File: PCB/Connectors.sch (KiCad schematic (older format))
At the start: 2 parts, among them P3 CONTROL, P4 MAIN_CONN

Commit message: Libraries and footprints adjustments. New connectors (4 pins main, 2 pins debug and 6 pins isp). New source input cap.
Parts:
- added P?: DEBUG TX/RX, symbol CONN_01X02
- added P?: ISP, symbol CONN_02X03
- P4: footprint Connectors_Molex:Molex_MiniFit-JR-5569-08A1_2x04x4.20mm_Angled -> Connectors_Molex:Molex_MiniFit-JR-5556-06A_2x03x4.20mm_Straight; symbol CONN_01X08 -> CONN_01X06
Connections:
- net +5V: now also P4.6 (P6), P?.2 (P2); no longer P4.1 (P1), P4.8 (P8)
- net CH0_OUT: now also P4.1 (P1); no longer P4.2 (P2)
- net CH0_PEDAL_SIG: now also P4.4 (P4); no longer P4.6 (P6)
- net CH1_OUT: now also P4.2 (P2); no longer P4.3 (P3)
- net CH1_PEDAL_SIG: now also P4.5 (P5); no longer P4.7 (P7)
- net GNDREF: now also P4.3 (P3), P?.6 (P6); no longer P4.4 (P4), P4.5 (P5)
- new net MISO: P?.1 (P1)
- new net MOSI: P?.4 (P4)
- new net RESET: P?.5 (P5)
- new net RX: P?.2 (P2)
- new net SCK: P?.3 (P3)
- new net TX: P?.1 (P1)
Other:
- moved on the sheet: P3
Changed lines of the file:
@@
 EESchema Schematic File Version 2
-LIBS:ArduBooster-rescue
 LIBS:power
 LIBS:device
@@
 Rev "1.0"
 Comp ""
-Comment1 ""
+Comment1 "Board connectors"
 Comment2 ""
 Comment3 ""
@@
 L CONN_01X05 P3
 U 1 1 54D7F0D9
-P 8200 3550
-F 0 "P3" H 8200 3850 50  0000 C CNN
-F 1 "CONTROL" V 8300 3550 50  0000 C CNN
-F 2 "Connect:Wafer_Horizontal15x5.8x7RM2.5-5" H 8200 3550 60  0001 C CNN
-F 3 "" H 8200 3550 60  0000 C CNN
-	1    8200 3550
+P 8200 4400
+F 0 "P3" H 8200 4700 50  0000 C CNN
+F 1 "CONTROL" V 8300 4400 50  0000 C CNN
+F 2 "Connect:Wafer_Horizontal15x5.8x7RM2.5-5" H 8200 4400 60  0001 C CNN
+F 3 "" H 8200 4400 60  0000 C CNN
+	1    8200 4400
 	1    0    0    1
 $EndComp
@@
 L GNDREF #PWR01
 U 1 1 54D7F247
-P 7850 3900
-F 0 "#PWR01" H 7850 3650 60  0001 C CNN
-F 1 "GNDREF" H 7850 3750 60  0000 C CNN
-F 2 "" H 7850 3900 60  0000 C CNN
-F 3 "" H 7850 3900 60  0000 C CNN
-	1    7850 3900
-	1    0    0    -1
-$EndComp
-Wire Wire Line
-	7850 3900 7850 3750
-Wire Wire Line
-	7850 3750 8000 3750
+P 7850 4750
+F 0 "#PWR01" H 7850 4500 60  0001 C CNN
+F 1 "GNDREF" H 7850 4600 60  0000 C CNN
+F 2 "" H 7850 4750 60  0000 C CNN
+F 3 "" H 7850 4750 60  0000 C CNN
+	1    7850 4750
+	1    0    0    -1
+$EndComp
+Wire Wire Line
+	7850 4750 7850 4600
+Wire Wire Line
+	7850 4600 8000 4600
 $Comp
 L +5V #PWR02
 U 1 1 54D7F26C
-P 7850 3200
-F 0 "#PWR02" H 7850 3050 60  0001 C CNN
-F 1 "+5V" H 7850 3340 60  0000 C CNN
-F 2 "" H 7850 3200 60  0000 C CNN
-F 3 "" H 7850 3200 60  0000 C CNN
-	1    7850 3200
-	1    0    0    -1
-$EndComp
-Wire Wire Line
-	8000 3350 7850 3350
-Wire Wire Line
-	7850 3350 7850 3200
-Wire Wire Line
-	7700 3650 8000 3650
-Wire Wire Line
-	7700 3550 8000 3550
-Text HLabel 7700 3450 0    60   Input ~ 0
+P 7850 4050
+F 0 "#PWR02" H 7850 3900 60  0001 C CNN
+F 1 "+5V" H 7850 4190 60  0000 C CNN
+F 2 "" H 7850 4050 60  0000 C CNN
+F 3 "" H 7850 4050 60  0000 C CNN
+	1    7850 4050
+	1    0    0    -1
+$EndComp
+Wire Wire Line
+	8000 4200 7850 4200
+Wire Wire Line
+	7850 4200 7850 4050
+Wire Wire Line
+	7700 4500 8000 4500
+Wire Wire Line
+	7700 4400 8000 4400
+Text HLabel 7700 4300 0    60   Input ~ 0
 SWITCH
 Wire Wire Line
-	7700 3450 8000 3450
-Text HLabel 7700 3650 0    60   Output ~ 0
+	7700 4300 8000 4300
+Text HLabel 7700 4500 0    60   Output ~ 0
 LED1
-Text HLabel 7700 3550 0    60   Output ~ 0
+Text HLabel 7700 4400 0    60   Output ~ 0
 LED2
-Text HLabel 4150 3650 2    60   Output ~ 0
+Text HLabel 4150 4500 2    60   Output ~ 0
 CH1_OUT
-Text HLabel 4150 3750 2    60   Output ~ 0
+Text HLabel 4150 4600 2    60   Output ~ 0
 CH0_OUT
-Text HLabel 4150 3250 2    60   Input ~ 0
+Text HLabel 4150 4200 2    60   Input ~ 0
 CH1_PEDAL_SIG
-Text HLabel 4150 3350 2    60   Input ~ 0
+Text HLabel 4150 4300 2    60   Input ~ 0
 CH0_PEDAL_SIG
 $Comp
-L CONN_01X08 P4
+L CONN_01X06 P4
 U 1 1 54E8D924
-P 3450 3500
-F 0 "P4" H 3450 3950 50  0000 C CNN
-F 1 "MAIN_CONN" V 3550 3500 50  0000 C CNN
-F 2 "Connectors_Molex:Molex_MiniFit-JR-5569-08A1_2x04x4.20mm_Angled" H 3450 3500 60  0001 C CNN
-F 3 "" H 3450 3500 60  0000 C CNN
-	1    3450 3500
+P 3450 4350
+F 0 "P4" H 3450 4800 50  0000 C CNN
+F 1 "MAIN_CONN" V 3550 4350 50  0000 C CNN
+F 2 "Connectors_Molex:Molex_MiniFit-JR-5556-06A_2x03x4.20mm_Straight" H 3450 4350 60  0001 C CNN
+F 3 "" H 3450 4350 60  0000 C CNN
+	1    3450 4350
 	-1   0    0    1
 $EndComp
@@
 L +5V #PWR03
 U 1 1 54E8E644
-P 3850 3000
-F 0 "#PWR03" H 3850 2850 60  0001 C CNN
-F 1 "+5V" H 3850 3140 60  0000 C CNN
-F 2 "" H 3850 3000 60  0000 C CNN
-F 3 "" H 3850 3000 60  0000 C CNN
-	1    3850 3000
+P 3850 3850
+F 0 "#PWR03" H 3850 3700 60  0001 C CNN
+F 1 "+5V" H 3850 3990 60  0000 C CNN
+F 2 "" H 3850 3850 60  0000 C CNN
+F 3 "" H 3850 3850 60  0000 C CNN
+	1    3850 3850
 	1    0    0    -1
 $EndComp
@@
 L PWR_FLAG #FLG04
 U 1 1 54E8E658
-P 4100 3000
-F 0 "#FLG04" H 4100 3095 30  0001 C CNN
-F 1 "PWR_FLAG" H 4100 3180 30  0000 C CNN
-F 2 "" H 4100 3000 60  0000 C CNN
-F 3 "" H 4100 3000 60  0000 C CNN
-	1    4100 3000
-	1    0    0    -1
-$EndComp
-Wire Wire Line
-	3650 3150 4100 3150
-Wire Wire Line
-	3850 3000 3850 3850
-Wire Wire Line
-	4100 3150 4100 3000
-Connection ~ 3850 3150
-Wire Wire Line
-	3850 3850 3650 3850
+P 4100 3850
+F 0 "#FLG04" H 4100 3945 30  0001 C CNN
+F 1 "PWR_FLAG" H 4100 4030 30  0000 C CNN
+F 2 "" H 4100 3850 60  0000 C CNN
+F 3 "" H 4100 3850 60  0000 C CNN
+	1    4100 3850
+	1    0    0    -1
+$EndComp
 $Comp
 L GNDREF #PWR05
 U 1 1 54E8E6DA
-P 3800 4050
-F 0 "#PWR05" H 3800 3800 60  0001 C CNN
-F 1 "GNDREF" H 3800 3900 60  0000 C CNN
-F 2 "" H 3800 4050 60  0000 C CNN
-F 3 "" H 3800 4050 60  0000 C CNN
-	1    3800 4050
+P 3800 4900
+F 0 "#PWR05" H 3800 4650 60  0001 C CNN
+F 1 "GNDREF" H 3800 4750 60  0000 C CNN
+F 2 "" H 3800 4900 60  0000 C CNN
+F 3 "" H 3800 4900 60  0000 C CNN
+	1    3800 4900
 	1    0    0    -1
 $EndComp
@@
 L PWR_FLAG #FLG06
 U 1 1 54E8E6F6
-P 4100 4050
-F 0 "#FLG06" H 4100 4145 30  0001 C CNN
-F 1 "PWR_FLAG" H 4100 4230 30  0000 C CNN
-F 2 "" H 4100 4050 60  0000 C CNN
-F 3 "" H 4100 4050 60  0000 C CNN
-	1    4100 4050
+P 4100 4900
+F 0 "#FLG06" H 4100 4995 30  0001 C CNN
+F 1 "PWR_FLAG" H 4100 5080 30  0000 C CNN
+F 2 "" H 4100 4900 60  0000 C CNN
+F 3 "" H 4100 4900 60  0000 C CNN
+	1    4100 4900
 	-1   0    0    1
 $EndComp
 Wire Wire Line
-	4100 4050 4100 4000
-Wire Wire Line
-	4100 4000 3800 4000
-Wire Wire Line
-	3800 3450 3800 4050
-Wire Wire Line
-	3650 3450 3800 3450
-Connection ~ 3800 4000
-Wire Wire Line
-	3650 3550 3800 3550
-Connection ~ 3800 3550
-Wire Wire Line
-	4150 3250 3650 3250
-Wire Wire Line
-	3650 3350 4150 3350
-Wire Wire Line
-	4150 3650 3650 3650
-Wire Wire Line
-	4150 3750 3650 3750
+	3650 4200 4150 4200
+Wire Wire Line
+	4150 4500 3650 4500
+Wire Wire Line
+	4150 4600 3650 4600
+Wire Wire Line
+	3650 4400 3800 4400
+Wire Wire Line
+	3800 4400 3800 4900
+Wire Wire Line
+	4100 4900 4100 4850
+Wire Wire Line
+	4100 4850 3800 4850
+Connection ~ 3800 4850
+Wire Wire Line
+	3650 4300 4150 4300
+Wire Wire Line
+	3850 3850 3850 4100
+Wire Wire Line
+	3850 4100 3650 4100
+Wire Wire Line
+	4100 3850 4100 3950
+Wire Wire Line
+	4100 3950 3850 3950
+Connection ~ 3850 3950
+$Comp
+L CONN_01X02 P?
+U 1 1 57BCD0AF
+P 8050 2650
+F 0 "P?" H 8050 2800 50  0000 C CNN
+F 1 "DEBUG TX/RX" V 8150 2650 50  0000 C CNN
+F 2 "" H 8050 2650 50  0000 C CNN
+F 3 "" H 8050 2650 50  0000 C CNN
+	1    8050 2650
+	1    0    0    -1
+$EndComp
+$Comp
+L CONN_02X03 P?
+U 1 1 57BCD0E6
+P 3850 2700
+F 0 "P?" H 3850 2900 50  0000 C CNN
+F 1 "ISP" H 3850 2500 50  0000 C CNN
+F 2 "" H 3850 1500 50  0000 C CNN
+F 3 "" H 3850 1500 50  0000 C CNN
+	1    3850 2700
+	1    0    0    -1
+$EndComp
+$Comp
+L +5V #PWR?
+U 1 1 57BCD18D
+P 4200 2500
+F 0 "#PWR?" H 4200 2350 60  0001 C CNN
+F 1 "+5V" H 4200 2640 60  0000 C CNN
+F 2 "" H 4200 2500 60  0000 C CNN
+F 3 "" H 4200 2500 60  0000 C CNN
+	1    4200 2500
+	1    0    0    -1
+$EndComp
+$Comp
+L GNDREF #PWR?
+U 1 1 57BCD1A8
+P 4200 2900
+F 0 "#PWR?" H 4200 2650 60  0001 C CNN
+F 1 "GNDREF" H 4200 2750 60  0000 C CNN
+F 2 "" H 4200 2900 60  0000 C CNN
+F 3 "" H 4200 2900 60  0000 C CNN
+	1    4200 2900
+	1    0    0    -1
+$EndComp
+Wire Wire Line
+	4100 2800 4200 2800
+Wire Wire Line
+	4200 2800 4200 2900
+Wire Wire Line
+	4200 2500 4200 2600
+Wire Wire Line
+	4200 2600 4100 2600
+Text HLabel 3200 2800 0    60   Output ~ 0
+RESET
+Wire Wire Line
+	3600 2800 3200 2800
+Text HLabel 3200 2700 0    60   Output ~ 0
+SCK
+Text HLabel 3200 2600 0    60   Input ~ 0
+MISO
+Wire Wire Line
+	3200 2600 3600 2600
+Wire Wire Line
+	3200 2700 3600 2700
+Text HLabel 4500 2700 2    60   Output ~ 0
+MOSI
+Wire Wire Line
+	4500 2700 4100 2700
+Text HLabel 7600 2600 0    60   Input ~ 0
+TX
+Wire Wire Line
+	7600 2600 7850 2600
+Text HLabel 7600 2700 0    60   Output ~ 0
+RX
+Wire Wire Line
+	7600 2700 7850 2700
 $EndSCHEMATC

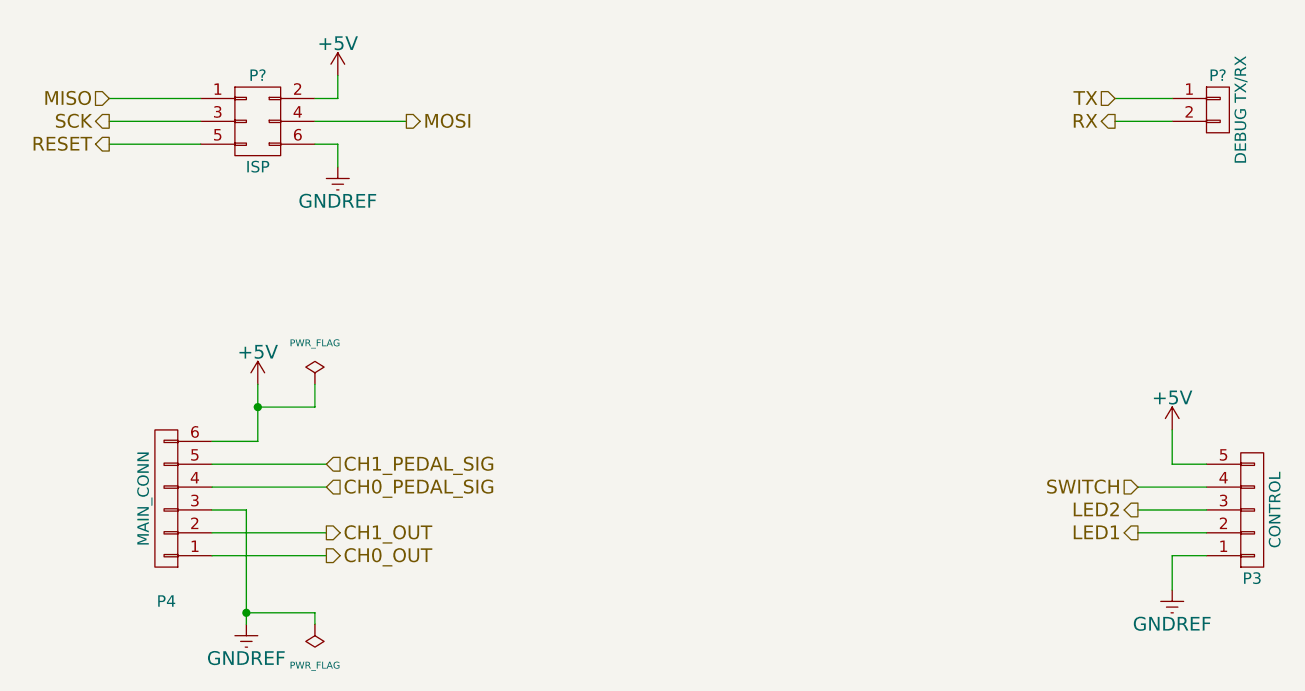
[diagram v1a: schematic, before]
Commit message: New connectors connection. Labels corrections (direction).
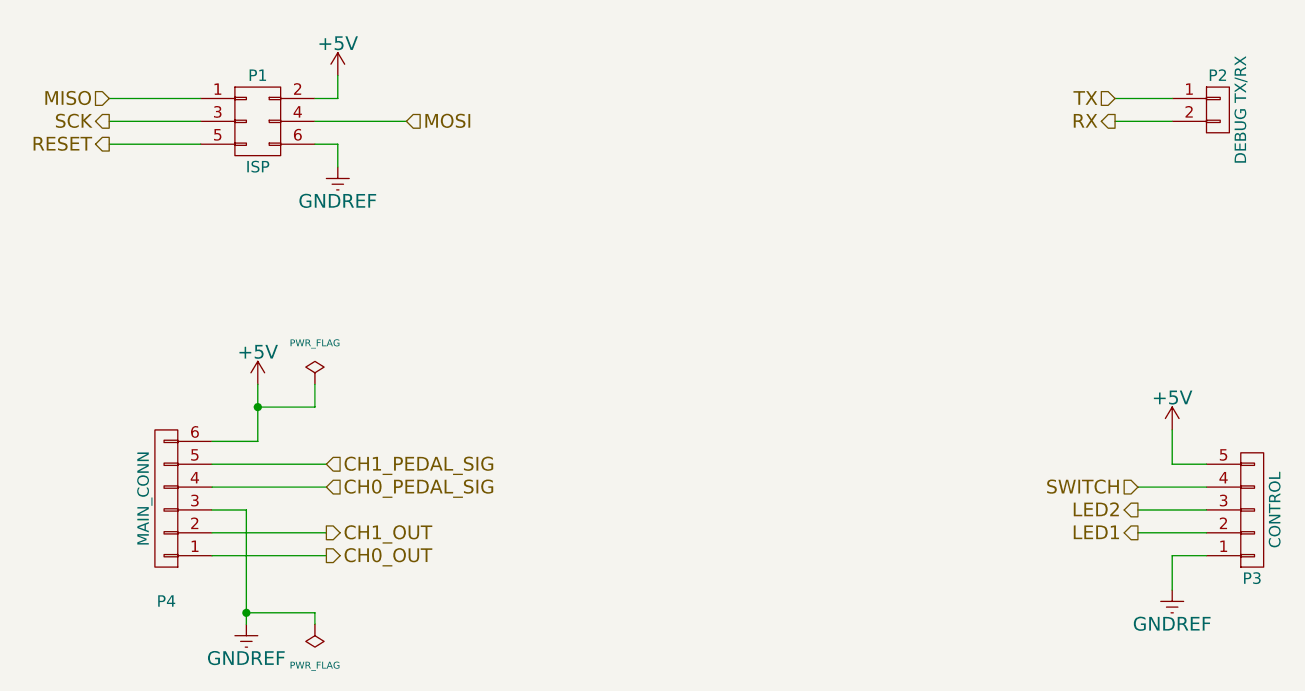
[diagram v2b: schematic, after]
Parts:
- gave numbers to parts that had none: 2
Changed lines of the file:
@@
 Connection ~ 3850 3950
 $Comp
-L CONN_01X02 P?
+L CONN_01X02 P2
 U 1 1 57BCD0AF
 P 8050 2650
-F 0 "P?" H 8050 2800 50  0000 C CNN
+F 0 "P2" H 8050 2800 50  0000 C CNN
 F 1 "DEBUG TX/RX" V 8150 2650 50  0000 C CNN
 F 2 "" H 8050 2650 50  0000 C CNN
@@
 $EndComp
 $Comp
-L CONN_02X03 P?
+L CONN_02X03 P1
 U 1 1 57BCD0E6
 P 3850 2700
-F 0 "P?" H 3850 2900 50  0000 C CNN
+F 0 "P1" H 3850 2900 50  0000 C CNN
 F 1 "ISP" H 3850 2500 50  0000 C CNN
 F 2 "" H 3850 1500 50  0000 C CNN
@@
 $EndComp
 $Comp
-L +5V #PWR?
+L +5V #PWR07
 U 1 1 57BCD18D
 P 4200 2500
-F 0 "#PWR?" H 4200 2350 60  0001 C CNN
+F 0 "#PWR07" H 4200 2350 60  0001 C CNN
 F 1 "+5V" H 4200 2640 60  0000 C CNN
 F 2 "" H 4200 2500 60  0000 C CNN
@@
 $EndComp
 $Comp
-L GNDREF #PWR?
+L GNDREF #PWR08
 U 1 1 57BCD1A8
 P 4200 2900
-F 0 "#PWR?" H 4200 2650 60  0001 C CNN
+F 0 "#PWR08" H 4200 2650 60  0001 C CNN
 F 1 "GNDREF" H 4200 2750 60  0000 C CNN
 F 2 "" H 4200 2900 60  0000 C CNN
@@
 Wire Wire Line
 	3200 2700 3600 2700
-Text HLabel 4500 2700 2    60   Output ~ 0
+Text HLabel 4500 2700 2    60   Input ~ 0
 MOSI
 Wire Wire Line
@@
 Text HLabel 7600 2600 0    60   Input ~ 0
 TX
-Wire Wire Line
-	7600 2600 7850 2600
 Text HLabel 7600 2700 0    60   Output ~ 0
 RX
 Wire Wire Line
 	7600 2700 7850 2700
+Wire Wire Line
+	7850 2600 7600 2600
 $EndSCHEMATC

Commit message: New connectors footprints. New .net file. New BoM file.
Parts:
- P1: footprint (none) -> Pin_Headers:Pin_Header_Straight_2x03
- P2: footprint (none) -> Pin_Headers:Pin_Header_Straight_1x02
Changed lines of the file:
@@
 F 0 "P2" H 8050 2800 50  0000 C CNN
 F 1 "DEBUG TX/RX" V 8150 2650 50  0000 C CNN
-F 2 "" H 8050 2650 50  0000 C CNN
+F 2 "Pin_Headers:Pin_Header_Straight_1x02" H 8050 2650 50  0001 C CNN
 F 3 "" H 8050 2650 50  0000 C CNN
 	1    8050 2650
@@
 F 0 "P1" H 3850 2900 50  0000 C CNN
 F 1 "ISP" H 3850 2500 50  0000 C CNN
-F 2 "" H 3850 1500 50  0000 C CNN
+F 2 "Pin_Headers:Pin_Header_Straight_2x03" H 3850 1500 50  0001 C CNN
 F 3 "" H 3850 1500 50  0000 C CNN
 	1    3850 2700

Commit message: Correct footprint main connector.
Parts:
- P4: footprint Connectors_Molex:Molex_MiniFit-JR-5556-06A_2x03x4.20mm_Straight -> Connectors_Molex:Molex_MiniFit-JR-5569-06A1_2x03x4.20mm_Angled
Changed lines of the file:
@@
 F 0 "P4" H 3450 4800 50  0000 C CNN
 F 1 "MAIN_CONN" V 3550 4350 50  0000 C CNN
-F 2 "Connectors_Molex:Molex_MiniFit-JR-5556-06A_2x03x4.20mm_Straight" H 3450 4350 60  0001 C CNN
+F 2 "Connectors_Molex:Molex_MiniFit-JR-5569-06A1_2x03x4.20mm_Angled" H 3450 4350 60  0001 C CNN
 F 3 "" H 3450 4350 60  0000 C CNN
 	1    3450 4350

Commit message: Last commit before Mux/Demux removel. Single layer PCB incompete (3 wires). Add ADC input filter.
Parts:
- P2: renamed from P1; footprint Pin_Headers:Pin_Header_Straight_2x03 -> Pin_Headers:Pin_Header_Straight_1x06_Pitch2.54mm; symbol CONN_02X03 -> CONN_01X06
- P3: renamed from P2; footprint Pin_Headers:Pin_Header_Straight_1x02 -> Pin_Headers:Pin_Header_Straight_1x02_Pitch2.54mm
- P4: renamed from P3; footprint Connect:Wafer_Horizontal15x5.8x7RM2.5-5 -> Connectors:Wafer_Horizontal15x5.8x7RM2.5-5
- renumbered P4 to P1
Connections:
- net GNDREF: now also P2.1 (P1); no longer P2.6 (P6)
- net MISO: now also P2.4 (P4); no longer P2.1 (P1)
- net MOSI: now also P2.5 (P5); no longer P2.4 (P4)
- net RESET: now also P2.6 (P6); no longer P2.5 (P5)
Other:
- moved on the sheet: P2
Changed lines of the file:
@@
 $EndDescr
 $Comp
-L CONN_01X05 P3
+L CONN_01X05 P4
 U 1 1 54D7F0D9
 P 8200 4400
-F 0 "P3" H 8200 4700 50  0000 C CNN
+F 0 "P4" H 8200 4700 50  0000 C CNN
 F 1 "CONTROL" V 8300 4400 50  0000 C CNN
-F 2 "Connect:Wafer_Horizontal15x5.8x7RM2.5-5" H 8200 4400 60  0001 C CNN
+F 2 "Connectors:Wafer_Horizontal15x5.8x7RM2.5-5" H 8200 4400 60  0001 C CNN
 F 3 "" H 8200 4400 60  0000 C CNN
 	1    8200 4400
@@
 	1    0    0    -1
 $EndComp
-Wire Wire Line
-	7850 4750 7850 4600
-Wire Wire Line
-	7850 4600 8000 4600
 $Comp
 L +5V #PWR02
@@
 	1    0    0    -1
 $EndComp
-Wire Wire Line
-	8000 4200 7850 4200
-Wire Wire Line
-	7850 4200 7850 4050
-Wire Wire Line
-	7700 4500 8000 4500
-Wire Wire Line
-	7700 4400 8000 4400
 Text HLabel 7700 4300 0    60   Input ~ 0
 SWITCH
-Wire Wire Line
-	7700 4300 8000 4300
 Text HLabel 7700 4500 0    60   Output ~ 0
 LED1
@@
 CH0_PEDAL_SIG
 $Comp
-L CONN_01X06 P4
+L CONN_01X06 P1
 U 1 1 54E8D924
 P 3450 4350
-F 0 "P4" H 3450 4800 50  0000 C CNN
+F 0 "P1" H 3450 4800 50  0000 C CNN
 F 1 "MAIN_CONN" V 3550 4350 50  0000 C CNN
 F 2 "Connectors_Molex:Molex_MiniFit-JR-5569-06A1_2x03x4.20mm_Angled" H 3450 4350 60  0001 C CNN
@@
 	-1   0    0    1
 $EndComp
-Wire Wire Line
-	3650 4200 4150 4200
-Wire Wire Line
-	4150 4500 3650 4500
-Wire Wire Line
-	4150 4600 3650 4600
-Wire Wire Line
-	3650 4400 3800 4400
-Wire Wire Line
-	3800 4400 3800 4900
-Wire Wire Line
-	4100 4900 4100 4850
-Wire Wire Line
-	4100 4850 3800 4850
-Connection ~ 3800 4850
-Wire Wire Line
-	3650 4300 4150 4300
-Wire Wire Line
-	3850 3850 3850 4100
-Wire Wire Line
-	3850 4100 3650 4100
-Wire Wire Line
-	4100 3850 4100 3950
-Wire Wire Line
-	4100 3950 3850 3950
-Connection ~ 3850 3950
-$Comp
-L CONN_01X02 P2
+$Comp
+L CONN_01X02 P3
 U 1 1 57BCD0AF
 P 8050 2650
-F 0 "P2" H 8050 2800 50  0000 C CNN
+F 0 "P3" H 8050 2800 50  0000 C CNN
 F 1 "DEBUG TX/RX" V 8150 2650 50  0000 C CNN
-F 2 "Pin_Headers:Pin_Header_Straight_1x02" H 8050 2650 50  0001 C CNN
+F 2 "Pin_Headers:Pin_Header_Straight_1x02_Pitch2.54mm" H 8050 2650 50  0001 C CNN
 F 3 "" H 8050 2650 50  0000 C CNN
 	1    8050 2650
@@
 $EndComp
 $Comp
-L CONN_02X03 P1
+L CONN_01X06 P2
 U 1 1 57BCD0E6
-P 3850 2700
-F 0 "P1" H 3850 2900 50  0000 C CNN
-F 1 "ISP" H 3850 2500 50  0000 C CNN
-F 2 "Pin_Headers:Pin_Header_Straight_2x03" H 3850 1500 50  0001 C CNN
-F 3 "" H 3850 1500 50  0000 C CNN
-	1    3850 2700
-	1    0    0    -1
+P 3800 2750
+F 0 "P2" H 3800 2950 50  0000 C CNN
+F 1 "ISP" H 3800 2550 50  0000 C CNN
+F 2 "Pin_Headers:Pin_Header_Straight_1x06_Pitch2.54mm" H 3800 1550 50  0001 C CNN
+F 3 "" H 3800 1550 50  0000 C CNN
+	1    3800 2750
+	-1   0    0    1
 $EndComp
 $Comp
 L +5V #PWR07
 U 1 1 57BCD18D
-P 4200 2500
-F 0 "#PWR07" H 4200 2350 60  0001 C CNN
-F 1 "+5V" H 4200 2640 60  0000 C CNN
-F 2 "" H 4200 2500 60  0000 C CNN
-F 3 "" H 4200 2500 60  0000 C CNN
-	1    4200 2500
-	1    0    0    -1
-$EndComp
-$Comp
-L GNDREF #PWR08
-U 1 1 57BCD1A8
-P 4200 2900
-F 0 "#PWR08" H 4200 2650 60  0001 C CNN
-F 1 "GNDREF" H 4200 2750 60  0000 C CNN
-F 2 "" H 4200 2900 60  0000 C CNN
-F 3 "" H 4200 2900 60  0000 C CNN
-	1    4200 2900
-	1    0    0    -1
-$EndComp
-Wire Wire Line
-	4100 2800 4200 2800
-Wire Wire Line
-	4200 2800 4200 2900
-Wire Wire Line
-	4200 2500 4200 2600
-Wire Wire Line
-	4200 2600 4100 2600
-Text HLabel 3200 2800 0    60   Output ~ 0
+P 4050 2450
+F 0 "#PWR07" H 4050 2300 60  0001 C CNN
+F 1 "+5V" H 4050 2590 60  0000 C CNN
+F 2 "" H 4050 2450 60  0000 C CNN
+F 3 "" H 4050 2450 60  0000 C CNN
+	1    4050 2450
+	1    0    0    -1
+$EndComp
+Text HLabel 4300 2500 2    60   Output ~ 0
 RESET
-Wire Wire Line
-	3600 2800 3200 2800
-Text HLabel 3200 2700 0    60   Output ~ 0
+Text HLabel 4300 2800 2    60   Output ~ 0
 SCK
-Text HLabel 3200 2600 0    60   Input ~ 0
+Text HLabel 4300 2700 2    60   Input ~ 0
 MISO
-Wire Wire Line
-	3200 2600 3600 2600
-Wire Wire Line
-	3200 2700 3600 2700
-Text HLabel 4500 2700 2    60   Input ~ 0
+Text HLabel 4300 2600 2    60   Input ~ 0
 MOSI
-Wire Wire Line
-	4500 2700 4100 2700
 Text HLabel 7600 2600 0    60   Input ~ 0
 TX
 Text HLabel 7600 2700 0    60   Output ~ 0
 RX
+$Comp
+L GNDREF #PWR08
+U 1 1 57BCD1A8
+P 4050 3050
+F 0 "#PWR08" H 4050 2800 60  0001 C CNN
+F 1 "GNDREF" H 4050 2900 60  0000 C CNN
+F 2 "" H 4050 3050 60  0000 C CNN
+F 3 "" H 4050 3050 60  0000 C CNN
+	1    4050 3050
+	1    0    0    -1
+$EndComp
+Wire Wire Line
+	7850 4750 7850 4600
+Wire Wire Line
+	7850 4600 8000 4600
+Wire Wire Line
+	8000 4200 7850 4200
+Wire Wire Line
+	7850 4200 7850 4050
+Wire Wire Line
+	7700 4500 8000 4500
+Wire Wire Line
+	7700 4400 8000 4400
+Wire Wire Line
+	7700 4300 8000 4300
+Wire Wire Line
+	3650 4200 4150 4200
+Wire Wire Line
+	4150 4500 3650 4500
+Wire Wire Line
+	4150 4600 3650 4600
+Wire Wire Line
+	3650 4400 3800 4400
+Wire Wire Line
+	3800 4400 3800 4900
+Wire Wire Line
+	4100 4900 4100 4850
+Wire Wire Line
+	4100 4850 3800 4850
+Connection ~ 3800 4850
+Wire Wire Line
+	3650 4300 4150 4300
+Wire Wire Line
+	3850 3850 3850 4100
+Wire Wire Line
+	3850 4100 3650 4100
+Wire Wire Line
+	4100 3850 4100 3950
+Wire Wire Line
+	4100 3950 3850 3950
+Connection ~ 3850 3950
 Wire Wire Line
 	7600 2700 7850 2700
 Wire Wire Line
 	7850 2600 7600 2600
+Wire Wire Line
+	4000 2800 4300 2800
+Wire Wire Line
+	4300 2700 4000 2700
+Wire Wire Line
+	4000 2600 4300 2600
+Wire Wire Line
+	4300 2500 4000 2500
+Wire Wire Line
+	4050 2450 4050 2900
+Wire Wire Line
+	4050 2900 4000 2900
+Wire Wire Line
+	4000 3000 4050 3000
+Wire Wire Line
+	4050 3000 4050 3050
 $EndSCHEMATC
